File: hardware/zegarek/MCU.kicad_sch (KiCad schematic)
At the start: 39 parts, among them J2 Conn_01x02, J3 Conn_01x02, J4 Conn_01x04, P1 USB_C_Plug_USB2.0, SW4 SW_Push, U4 STM32F091RCTx, U5 CH340C, Y1 32.768kHz

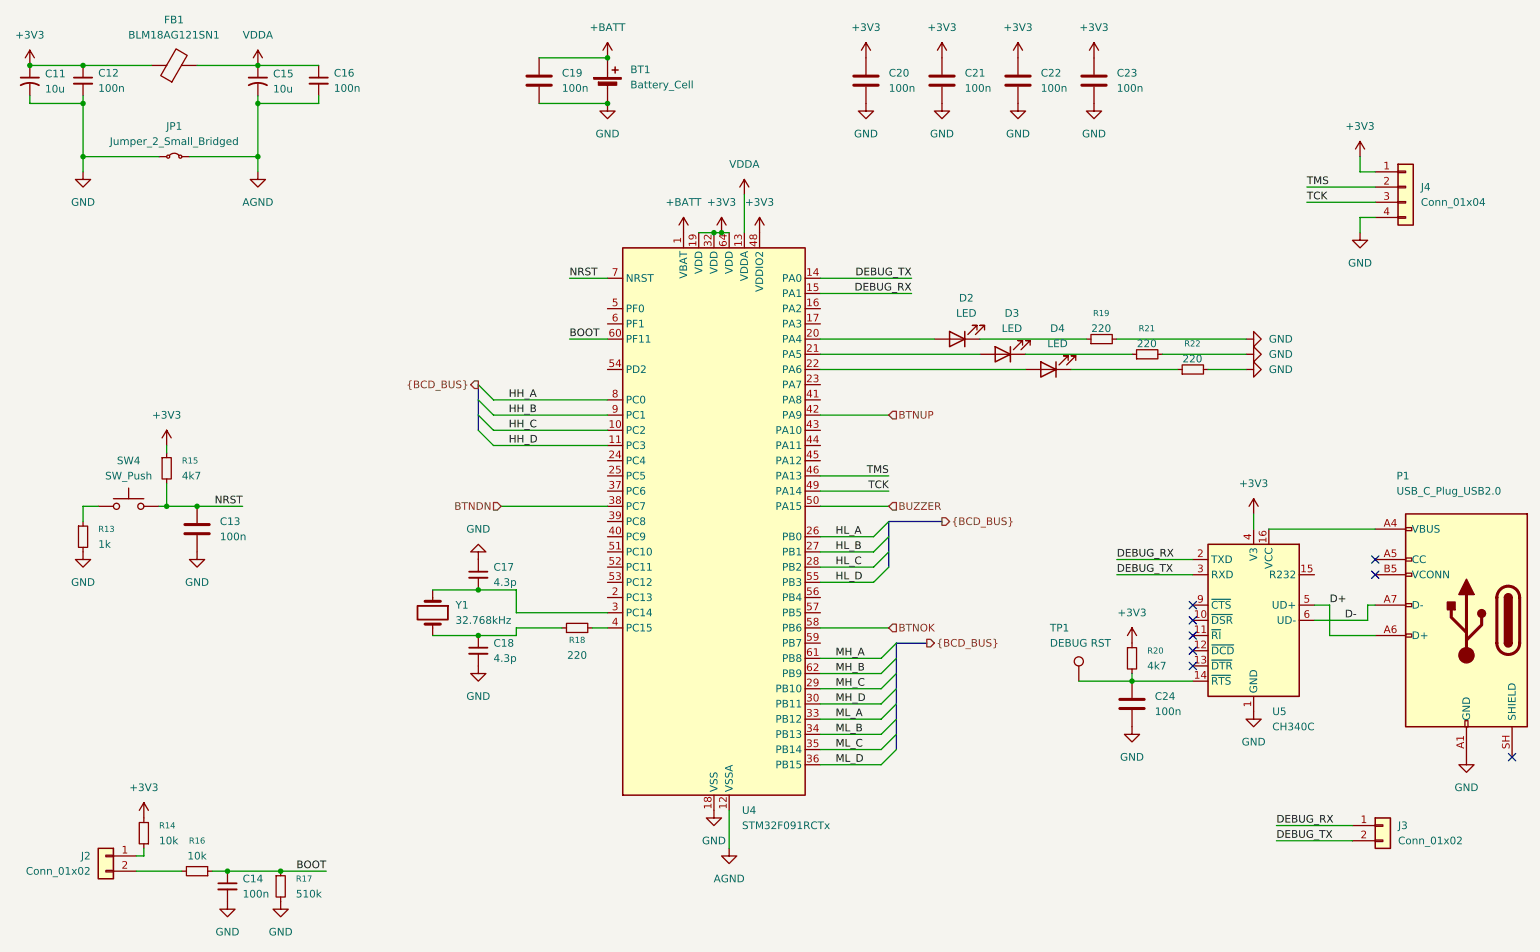
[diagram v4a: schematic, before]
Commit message: new revision with fixes from prototype: level shift to mcu added, changed con footprints and debug usb deleted
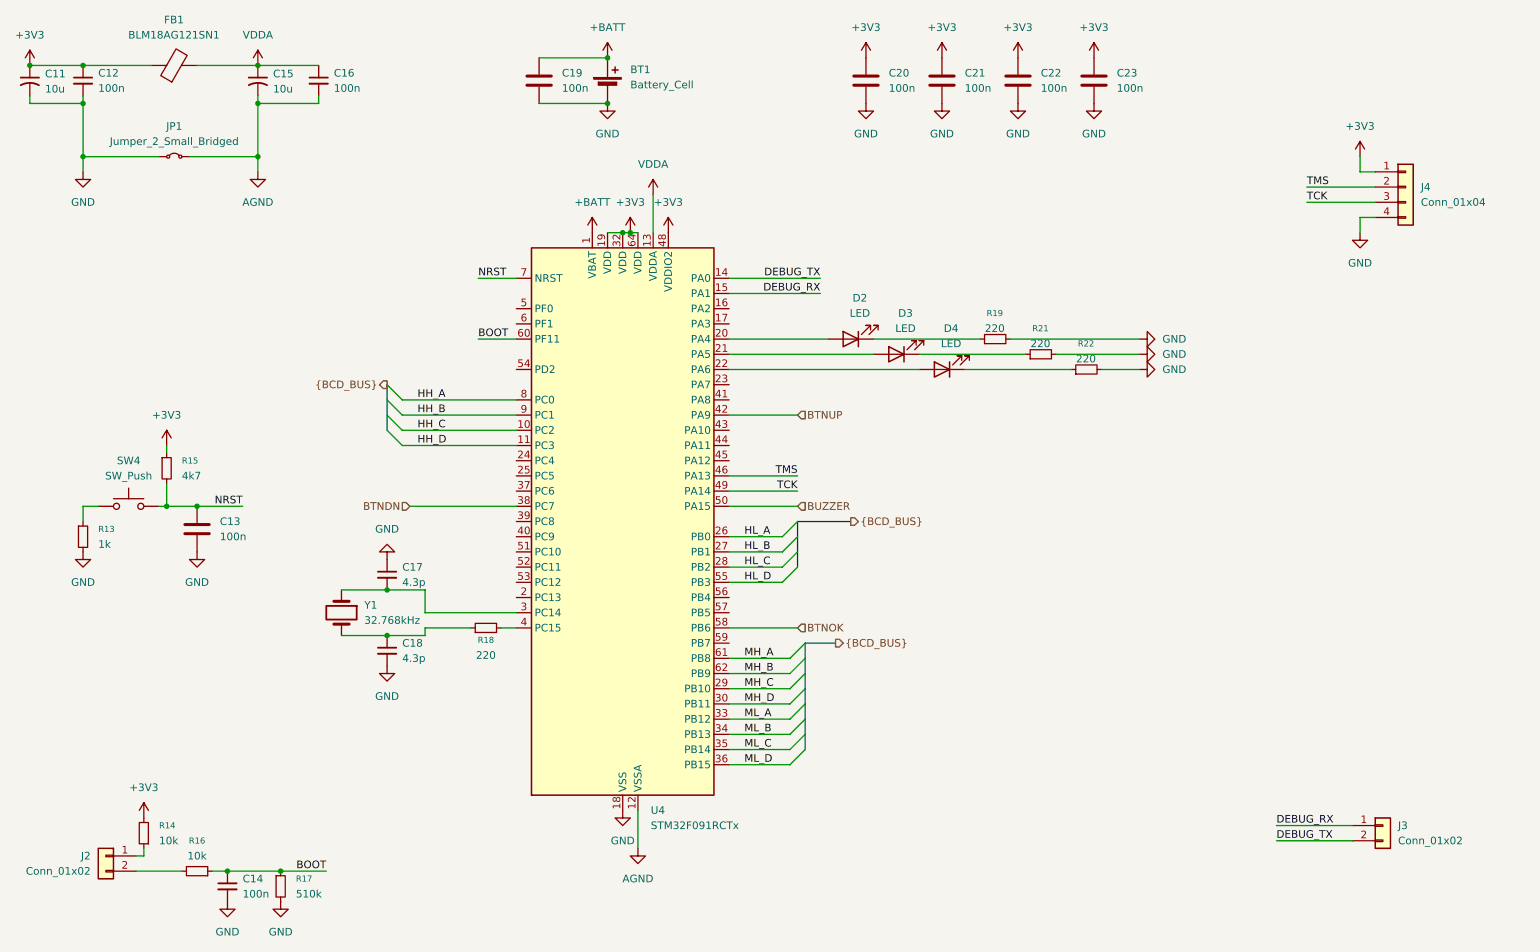
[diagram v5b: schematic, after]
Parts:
- removed C24: 100n, Capacitor_SMD:C_1206_3216Metric_Pad1.33x1.80mm_HandSolder, symbol Device:C
- removed P1: USB_C_Plug_USB2.0, Connector_USB:USB_C_Receptacle_Amphenol_12401948E412A, symbol Connector:USB_C_Plug_USB2.0
- removed R20: 4k7, Resistor_SMD:R_0603_1608Metric_Pad0.98x0.95mm_HandSolder, symbol Device:R_Small
- removed TP1: DEBUG RST, TestPoint:TestPoint_Loop_D2.60mm_Drill0.9mm_Beaded, symbol Connector:TestPoint
- removed U5: CH340C, Package_SO:SOIC-16_3.9x9.9mm_P1.27mm, symbol Interface_USB:CH340C
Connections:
- no-connect marks 8 -> 0
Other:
- moved on the sheet: C17, C18, D2, D3, D4, R18, R19, R21, R22, U4, Y1

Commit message: correction changes, postprod files regenration,added OE and EN to MCU schematic
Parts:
- added R44: 1k, symbol Device:R_Small
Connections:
- net at U4.24 (PC4): now also R44.2
- new net ~{OE}: R44.1
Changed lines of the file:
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@@
+	(wire
+		(pts
+			(xy 104.14 93.98) (xy 109.22 93.98)
+		)
+		(stroke
+			(width 0)
+			(type default)
+		)
+	)
 	(wire
 		(pts
@@
 			)
 			(justify left)
+		)
+	)
+	(hierarchical_label "~{OE}"
+		(shape input)
+		(at 99.06 93.98 180)
+		(effects
+			(font
+				(size 1.27 1.27)
+			)
+			(justify right)
 		)
 	)
@@
 					(unit 1)
 				)
+			)
+		)
+	)
+	(symbol
+		(lib_id "Device:R_Small")
+		(at 101.6 93.98 90)
+		(mirror x)
+		(unit 1)
+		(body_style 1)
+		(exclude_from_sim no)
+		(in_bom yes)
+		(on_board yes)
+		(in_pos_files yes)
+		(dnp no)
+		(property "Reference" "R44"
+			(at 101.6 99.06 90)
+			(show_name no)
+			(do_not_autoplace no)
+			(effects
+				(font
+					(size 1.016 1.016)
+				)
+			)
+		)
+		(property "Value" "1k"
+			(at 101.6 96.52 90)
+			(show_name no)
+			(do_not_autoplace no)
+			(effects
+				(font
+					(size 1.27 1.27)
+				)
+			)
+		)
+		(property "Footprint" ""
+			(at 101.6 93.98 0)
+			(hide yes)
+			(show_name no)
+			(do_not_autoplace no)
+			(effects
+				(font
+					(size 1.27 1.27)
+				)
+			)
+		)
+		(property "Datasheet" ""
+			(at 101.6 93.98 0)
+			(hide yes)
+			(show_name no)
+			(do_not_autoplace no)
+			(effects
+				(font
+					(size 1.27 1.27)
+				)
+			)
+		)
+		(property "Description" "Resistor, small symbol"
+			(at 101.6 93.98 0)
+			(hide yes)
+			(show_name no)
+			(do_not_autoplace no)
+			(effects
+				(font
+					(size 1.27 1.27)
+				)
+			)
+		)
+		(pin "1"
+		)
+		(pin "2"
+		)
+		(instances
+			(project "zegarek"
+				(path "/f4008fb9-ad6b-45c6-9bc0-571e7640a726/209f222f-184e-41c4-8d66-9f0390d2086f"
+					(reference "R44")
+					(unit 1)
+				)

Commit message: reqenerating postprod
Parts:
- added R47: 1k, Resistor_SMD:R_0603_1608Metric_Pad0.98x0.95mm_HandSolder, symbol Device:R_Small
- C17, C18: value 4.3p -> 4.3p?
- R15: value 4k7 -> 10k
- R44: footprint (none) -> Resistor_SMD:R_0603_1608Metric_Pad0.98x0.95mm_HandSolder
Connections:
- net at U4.25 (PC5): now also R47.2
- net ~{OE} renamed MIN_~{OE}
- new net HOUR_~{OE}: R47.1
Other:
- moved on the sheet: R15
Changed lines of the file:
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@@
 	)
 	(junction
-		(at 50.8 101.6)
-		(diameter 0)
-		(color 0 0 0 0)
-	)
-	(junction
 		(at 36.83 27.94)
 		(diameter 0)
@@
 	(wire
 		(pts
-			(xy 50.8 101.6) (xy 49.53 101.6)
+			(xy 49.53 101.6) (xy 55.88 101.6)
 		)
 		(stroke
@@
 	(wire
 		(pts
-			(xy 50.8 97.79) (xy 50.8 101.6)
+			(xy 55.88 97.79) (xy 55.88 101.6)
 		)
 		(stroke
@@
 	(wire
 		(pts
+			(xy 91.44 93.98) (xy 99.06 93.98)
+		)
+		(stroke
+			(width 0)
+			(type default)
+		)
+	)
+	(wire
+		(pts
 			(xy 168.91 73.66) (xy 186.69 73.66)
 		)
@@
 	(wire
 		(pts
+			(xy 91.44 96.52) (xy 92.71 96.52)
+		)
+		(stroke
+			(width 0)
+			(type default)
+		)
+	)
+	(wire
+		(pts
 			(xy 106.68 121.92) (xy 109.22 121.92)
 		)
@@
 	(wire
 		(pts
-			(xy 50.8 101.6) (xy 55.88 101.6)
-		)
-		(stroke
-			(width 0)
-			(type default)
-		)
-	)
-	(wire
-		(pts
 			(xy 102.87 73.66) (xy 109.22 73.66)
 		)
@@
 	(wire
 		(pts
-			(xy 50.8 91.44) (xy 50.8 92.71)
+			(xy 55.88 91.44) (xy 55.88 92.71)
 		)
 		(stroke
@@
 		)
 	)
+	(wire
+		(pts
+			(xy 97.79 96.52) (xy 109.22 96.52)
+		)
+		(stroke
+			(width 0)
+			(type default)
+		)
+	)
 	(label "MH_A"
 		(at 147.32 127 0)
@@
 		)
 	)
+	(hierarchical_label "HOUR_~{OE}"
+		(shape input)
+		(at 91.44 96.52 180)
+		(effects
+			(font
+				(size 1.27 1.27)
+			)
+			(justify right)
+		)
+	)
 	(hierarchical_label "{BCD_BUS}"
 		(shape output)
@@
 		)
 	)
-	(hierarchical_label "{BCD_BUS}"
-		(shape output)
-		(at 87.63 81.28 180)
+	(hierarchical_label "MIN_~{OE}"
+		(shape input)
+		(at 91.44 93.98 180)
 		(effects
 			(font
@@
 		)
 	)
-	(hierarchical_label "BTNOK"
-		(shape input)
-		(at 156.21 121.92 0)
+	(hierarchical_label "{BCD_BUS}"
+		(shape output)
+		(at 87.63 81.28 180)
 		(effects
 			(font
 				(size 1.27 1.27)
 			)
-			(justify left)
+			(justify right)
 		)
 	)
-	(hierarchical_label "~{OE}"
+	(hierarchical_label "BTNOK"
 		(shape input)
-		(at 99.06 93.98 180)
+		(at 156.21 121.92 0)
 		(effects
 			(font
 				(size 1.27 1.27)
 			)
-			(justify right)
+			(justify left)
 		)
 	)
@@
 	)
 	(symbol
+		(lib_id "Device:R_Small")
+		(at 95.25 96.52 90)
+		(mirror x)
+		(unit 1)
+		(body_style 1)
+		(exclude_from_sim no)
+		(in_bom yes)
+		(on_board yes)
+		(in_pos_files yes)
+		(dnp no)
+		(property "Reference" "R47"
+			(at 95.25 100.838 90)
+			(show_name no)
+			(do_not_autoplace no)
+			(effects
+				(font
+					(size 1.016 1.016)
+				)
+			)
+		)
+		(property "Value" "1k"
+			(at 95.25 98.298 90)
+			(show_name no)
+			(do_not_autoplace no)
+			(effects
+				(font
+					(size 1.27 1.27)
+				)
+			)
+		)
+		(property "Footprint" "Resistor_SMD:R_0603_1608Metric_Pad0.98x0.95mm_HandSolder"
+			(at 95.25 96.52 0)
+			(hide yes)
+			(show_name no)
+			(do_not_autoplace no)
+			(effects
+				(font
+					(size 1.27 1.27)
+				)
+			)
+		)
+		(property "Datasheet" ""
+			(at 95.25 96.52 0)
+			(hide yes)
+			(show_name no)
+			(do_not_autoplace no)
+			(effects
+				(font
+					(size 1.27 1.27)
+				)
+			)
+		)
+		(property "Description" "Resistor, small symbol"
+			(at 95.25 96.52 0)
+			(hide yes)
+			(show_name no)
+			(do_not_autoplace no)
+			(effects
+				(font
+					(size 1.27 1.27)
+				)
+			)
+		)
+		(pin "1"
+		)
+		(pin "2"
+		)
+		(instances
+			(project "zegarek"
+				(path "/f4008fb9-ad6b-45c6-9bc0-571e7640a726/209f222f-184e-41c4-8d66-9f0390d2086f"
+					(reference "R47")
+					(unit 1)
+				)
+			)
+		)
+	)
+	(symbol
 		(lib_id "power:GND")
 		(at 180.34 34.29 0)
@@
 	(symbol
 		(lib_id "Device:R_Small")
-		(at 50.8 95.25 0)
+		(at 55.88 95.25 0)
 		(unit 1)
 		(body_style 1)
@@
 		(fields_autoplaced yes)
 		(property "Reference" "R15"
-			(at 53.34 93.9799 0)
+			(at 58.42 93.9799 0)
 			(show_name no)
 			(do_not_autoplace no)
@@
 			)
 		)
-		(property "Value" "4k7"
-			(at 53.34 96.5199 0)
+		(property "Value" "10k"
+			(at 58.42 96.5199 0)
 			(show_name no)
 			(do_not_autoplace no)
@@
 		)
 		(property "Footprint" "Resistor_SMD:R_0603_1608Metric_Pad0.98x0.95mm_HandSolder"
-			(at 50.8 95.25 0)
+			(at 55.88 95.25 0)
 			(hide yes)
 			(show_name no)
@@
 		)
 		(property "Datasheet" ""
-			(at 50.8 95.25 0)
+			(at 55.88 95.25 0)
 			(hide yes)
 			(show_name no)
@@
 		)
 		(property "Description" "Resistor, small symbol"
-			(at 50.8 95.25 0)
+			(at 55.88 95.25 0)
 			(hide yes)
 			(show_name no)
@@
 		)
 		(property "LCSC" "C3152147"
-			(at 53.34 93.9799 0)
+			(at 58.42 93.9799 0)
 			(hide yes)
 			(show_name no)
@@
 			)
 		)
-		(property "Value" "4.3p"
+		(property "Value" "4.3p?"
 			(at 90.17 114.3062 0)
 			(show_name no)
@@
 		(dnp no)
 		(property "Reference" "R44"
-			(at 101.6 99.06 90)
+			(at 101.6 98.298 90)
 			(show_name no)
 			(do_not_autoplace no)
@@
 		)
 		(property "Value" "1k"
-			(at 101.6 96.52 90)
+			(at 101.6 95.758 90)
 			(show_name no)
 			(do_not_autoplace no)
@@
 			)
 		)
-		(property "Footprint" ""
+		(property "Footprint" "Resistor_SMD:R_0603_1608Metric_Pad0.98x0.95mm_HandSolder"
 			(at 101.6 93.98 0)
 			(hide yes)
@@
 			)
 		)
-		(property "Value" "4.3p"
+		(property "Value" "4.3p?"
 			(at 90.17 127.0062 0)
 			(show_name no)
@@
 	(symbol
 		(lib_id "power:+3V3")
-		(at 50.8 91.44 0)
+		(at 55.88 91.44 0)
 		(unit 1)
 		(body_style 1)
@@
 		(fields_autoplaced yes)
 		(property "Reference" "#PWR032"
-			(at 50.8 95.25 0)
+			(at 55.88 95.25 0)
 			(hide yes)
 			(show_name no)
@@
 		)
 		(property "Value" "+3V3"
-			(at 50.8 86.36 0)
+			(at 55.88 86.36 0)
 			(show_name no)
 			(do_not_autoplace no)
@@
 		)
 		(property "Footprint" ""
-			(at 50.8 91.44 0)
+			(at 55.88 91.44 0)
 			(hide yes)
 			(show_name no)
@@
 		)
 		(property "Datasheet" ""
-			(at 50.8 91.44 0)
+			(at 55.88 91.44 0)
 			(hide yes)
 			(show_name no)
@@
 		)
 		(property "Description" "Power symbol creates a global label with name \"+3V3\""
-			(at 50.8 91.44 0)
+			(at 55.88 91.44 0)
 			(hide yes)
 			(show_name no)
